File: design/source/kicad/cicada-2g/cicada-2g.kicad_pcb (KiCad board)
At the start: 2 copper layers, 40 x 65 mm, 52 parts, among them J2 Host, J3 USB_OTG, J4 IPX, J5 IPX, P1 SK-C793, Q1 NMOS, Q2 NMOS, Q4 NMOS, U2 USBLC6-2SC6, U3 M3406-ADJ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

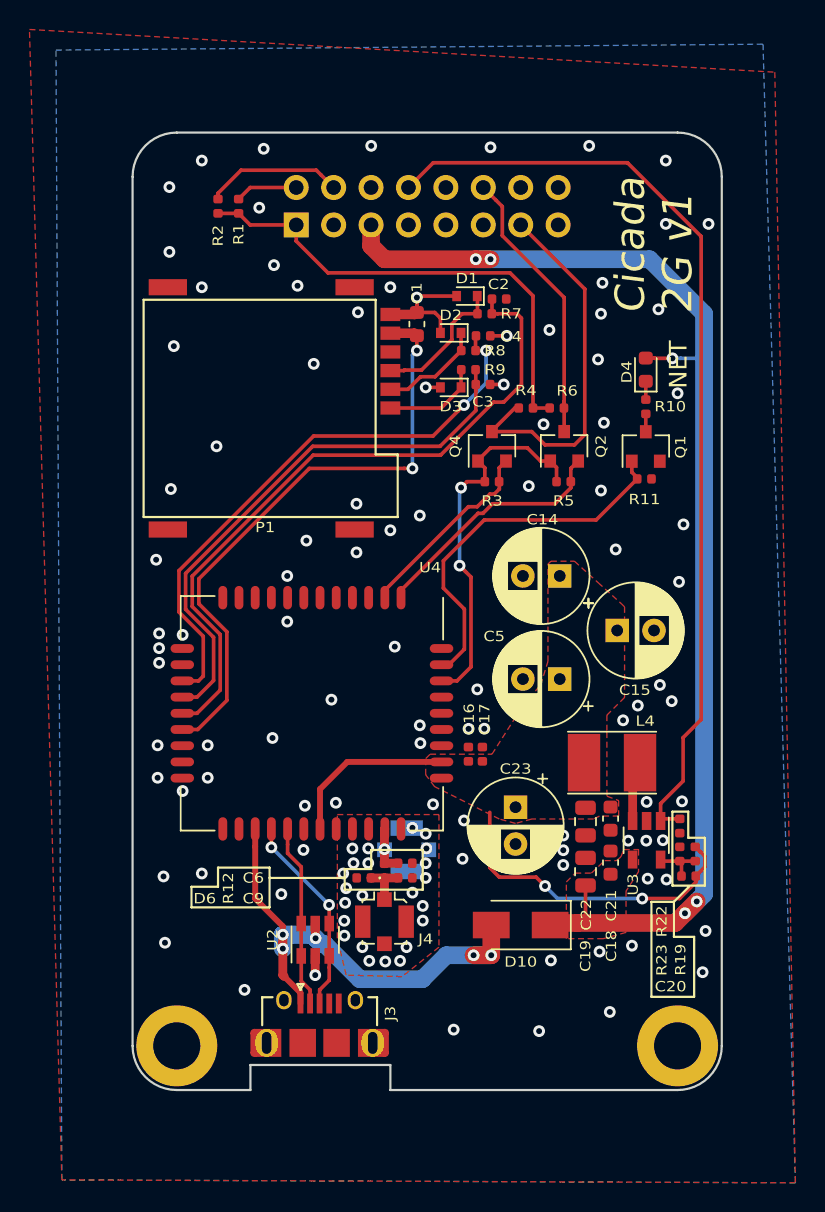
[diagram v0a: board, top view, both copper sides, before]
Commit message: Cicada 2G v2.1 - don't swap RX-TX
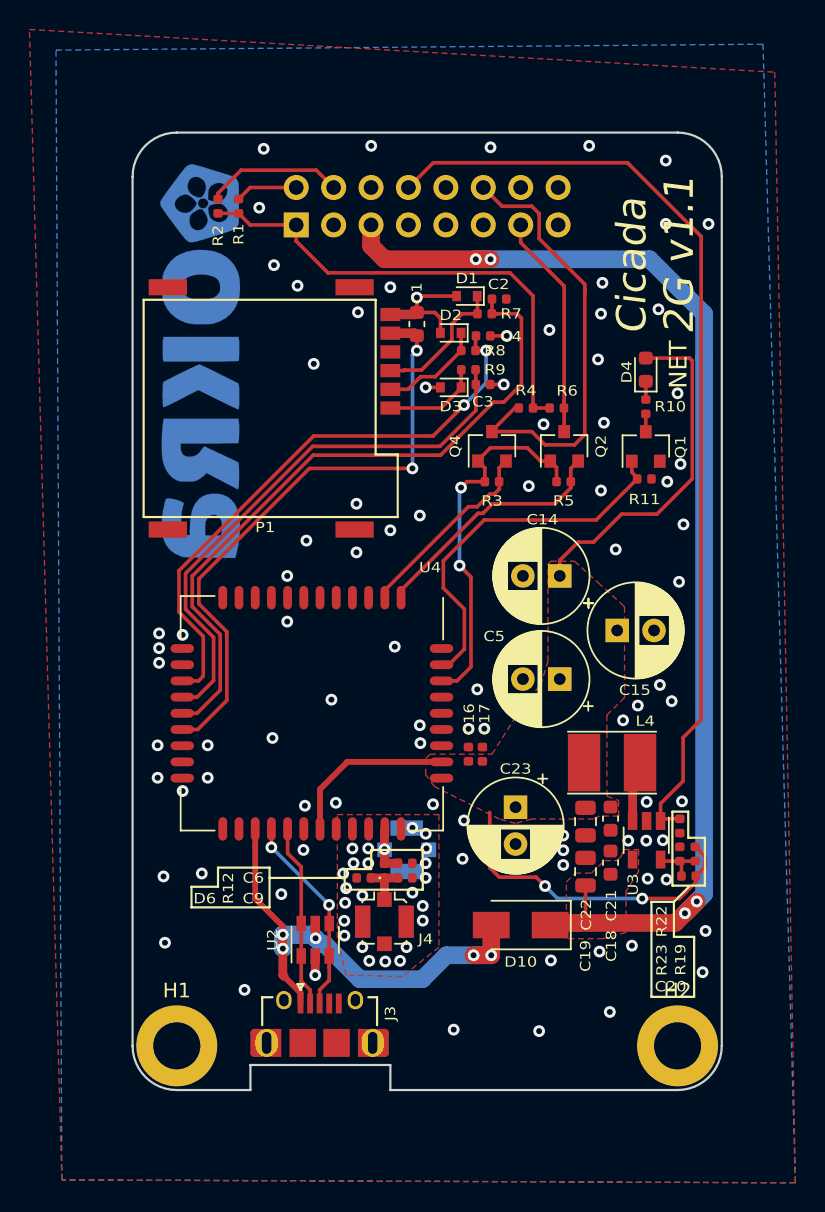
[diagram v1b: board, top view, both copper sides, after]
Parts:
- added LOGO1: SYM_Hot_Small, cicada-footprints:okra_logo_copper_2, B.Cu at (115.6, 75.5)
- R10: value 220R -> 470R
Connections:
- D4 pad 2: /5v -> /V_BATT
- Q2 pad 3: /UART_RX_3v3 -> /UART_TX_3v3
- Q4 pad 3: /UART_TX_3v3 -> /UART_RX_3v3
- R4 pad 2: /UART_TX_3v3 -> /UART_RX_3v3
- R6 pad 2: /UART_RX_3v3 -> /UART_TX_3v3
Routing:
- net /V_BATT: track 33.7 -> 57.3 mm
- net /UART_RX_3v3: track 18.9 -> 30.6 mm
- net /UART_TX_3v3: track 25.5 -> 15.3 mm
- net /5v: track 85.5 -> 81.6 mm, vias 5 -> 4
- net GND: vias 119 -> 113
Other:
- board text added: "Cicada 2G v1.1"
- board text removed: "Cicada 2G v1"

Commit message: Remove OKRA logo from PCB
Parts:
- removed LOGO1: SYM_Hot_Small, cicada-footprints:okra_logo_copper_2

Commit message: Updated PCB
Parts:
- removed C15, C23: 330uF 6.3v, Capacitor_THT:CP_Radial_D6.3mm_P2.50mm
- removed Q2, Q4: NMOS, Package_TO_SOT_SMD:SOT-23
- removed R11: 40.2k, Resistor_SMD:R_0402_1005Metric
- removed R5, R6: 4.7k, Resistor_SMD:R_0402_1005Metric
- added  : TestPoint, TestPoint:TestPoint_Pad_D1.5mm, F.Cu at (149.5, 78.8)
- added 5V: TestPoint, TestPoint:TestPoint_Pad_D1.5mm, F.Cu at (130.0, 68.8)
- added C10: 1000uF 10v, Capacitor_THT:CP_Radial_D8.0mm_P3.50mm, F.Cu at (148.3, 91.2)
- added C11: 1000uF 10v, Capacitor_THT:CP_Radial_D8.0mm_P3.50mm, F.Cu at (139.9, 98.0)
- added C12: 1000uF 10v, Capacitor_THT:CP_Radial_D8.0mm_P3.50mm, F.Cu at (145.6, 82.9)
- added C7: DNP, Capacitor_SMD:C_0402_1005Metric, F.Cu at (126.4, 89.6)
- added C8: DNP, Capacitor_SMD:C_0402_1005Metric, F.Cu at (136.1, 82.8)
- added D5: M2, Diode_SMD:D_SMA, F.Cu at (137.3, 118.7)
- added LOGO1: SYM_Hot_Small, cicada-footprints:okra_logo_copper_2, B.Cu at (115.3, 75.5)
- added R13: 0R, Resistor_SMD:R_0402_1005Metric, F.Cu at (134.8, 93.8)
- added R14: 6.98k, Resistor_SMD:R_0402_1005Metric, F.Cu at (142.8, 117.7)
- added TP1: TestPoint, TestPoint:TestPoint_Pad_D1.5mm, F.Cu at (131.5, 89.1)
- added U1: 74LVC1G17, Package_TO_SOT_SMD:SOT-353_SC-70-5, F.Cu at (134.0, 84.0)
- added U5: 74LVC1G17, Package_TO_SOT_SMD:SOT-353_SC-70-5, F.Cu at (130.7, 85.4)
- added V_BATT: TestPoint, TestPoint:TestPoint_Pad_D1.5mm, F.Cu at (138.4, 110.5)
- C14, C5: value 330uF 6.3v -> 1000uF 10v; footprint Capacitor_THT:CP_Radial_D6.3mm_P2.50mm -> Capacitor_THT:CP_Radial_D8.0mm_P3.50mm
- J2: footprint Connector_PinSocket_2.54mm:PinSocket_2x08_P2.54mm_Vertical -> Connector_PinSocket_2.54mm:PinSocket_2x10_P2.54mm_Vertical
- Q1: value NMOS -> BC847C
- R1: value DNP -> 150k
- R10: value 470R -> 330R
- R2: value 340k -> 150k
- R3, R4: value 4.7k -> 330R
- moved R3 9.35 mm to (128.1, 89.5), turned to 270 degrees
- moved C5 8.66 mm to (148.3, 99.7)
- moved R2 8.50 mm to (124.6, 61.7), turned to 0 degrees
- moved Q1 8.10 mm to (141.4, 74.5), turned to 0 degrees
- moved C22 6.73 mm to (135.1, 107.5)
- moved C21 6.70 mm to (136.8, 107.7)
- moved R10 5.60 mm to (140.4, 77.3)
- moved R1 5.53 mm to (122.6, 61.7), turned to 180 degrees
- moved L4 3.99 mm to (140.9, 105.8)
- moved R4 3.85 mm to (134.9, 81.4), turned to 270 degrees
- moved J2 2.54 mm to (119.6, 66.3)
- moved D4 1.66 mm to (144.3, 75.4), turned to 270 degrees
- moved C14 0.60 mm to (139.9, 89.5)
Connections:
- C5 pad 1: /V_BATT -> /5v
- J2 pad 1: /3v3 -> Net-(J2-Pad1)
- J2 pad 10: /SPI_CLK_3v3 -> /POWER
- J2 pad 11: /SPI_MOSI_3v3 -> /SPI_MISO_3v3
- J2 pad 12: /UART_RX_3v3 -> /SPI_CLK_3v3
- J2 pad 13: /UART_TX_3v3 -> /SPI_MOSI_3v3
- J2 pad 14: /nCS_WIFI -> /UART_RX_3v3
- J2 pad 15: /nCS_3G_3v3 -> /UART_TX_3v3
- J2 pad 16: /nRST -> /nCS_WIFI
- J2 pad 2: /VER_1 -> Net-(J2-Pad2)
- J2 pad 3: GND -> /3v3
- J2 pad 4: /VER_2 -> /VER_1
- J2 pad 5: /5v -> GND
- J2 pad 6: GND -> /VER_2
- J2 pad 7: GND -> /5v
- J2 pad 8: /POWER -> GND
- J2 pad 9: /SPI_MISO_3v3 -> GND
- Q1 pad 2: GND -> Net-(Q1-Pad2)
- Q1 pad 3: Net-(Q1-Pad3) -> Net-(D4-Pad1)
- R10 pad 1: Net-(D4-Pad1) -> Net-(Q1-Pad2)
- R10 pad 2: Net-(Q1-Pad3) -> GND
- R3 pad 1: /2v8 -> Net-(R3-Pad1)
- R4 pad 1: /3v3 -> /UART_TX_3v3
- R4 pad 2: /UART_RX_3v3 -> Net-(R4-Pad2)
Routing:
- net /5v: track 81.6 -> 224.7 mm, vias 4 -> 6
- net /POWER: track 64.8 -> 80.9 mm, vias 0 -> 1
- net /UART_RX_2v8: track 13.2 -> 2.91 mm
- net /2v8: track 25.6 -> 15.9 mm
- net /V_BATT: track 57.3 -> 48.4 mm
- net /VER_2: track 9.38 -> 2.22 mm
- net /UART_TX_2v8: track 16.9 -> 9.86 mm
- net Net-(TP1-Pad1): track 0.00 -> 6.09 mm
- net Net-(R13-Pad1): track 0.00 -> 5.48 mm
- net /UART_RX_3v3: track 30.6 -> 25.2 mm
- net Net-(R3-Pad1): track 0.00 -> 4.22 mm
- net GND: track 12.7 -> 16.4 mm, vias 113 -> 111
- net Net-(D5-Pad1): track 0.00 -> 3.37 mm
- net /UART_TX_3v3: track 15.3 -> 18.5 mm
- net /VBUS: track 36.5 -> 39.3 mm
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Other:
- board text added: "Cicada 2G v1.2"
- board text removed: "Cicada 2G v1.1"

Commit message: Generated manufacturing package
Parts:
- C10: value 1000uF 10v -> DNP 1000uF 10v
- D5: value M2 -> SS14
- J5: value IPX -> DNP IPX
- Q1: value BC847C -> 2N7002
- R10: value 330R -> 1K
- TP2: renamed from  
- moved LOGO1 3.80 mm to (114.6, 79.3)
- renumbered 5V to TP3, V_BATT to TP4
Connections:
- Q1 pad 2: Net-(Q1-Pad2) -> GND
- Q1 pad 3: Net-(D4-Pad1) -> Net-(Q1-Pad3)
- R10 pad 1: Net-(Q1-Pad2) -> Net-(Q1-Pad3)
- R10 pad 2: GND -> Net-(D4-Pad1)
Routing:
- net GND: track 16.4 -> 22.8 mm, vias 111 -> 112
- net Net-(D4-Pad1): track 1.95 -> 5.85 mm
- net Net-(Q1-Pad3): track 0.00 -> 3.77 mm
- net Net-(Q1-Pad2): track 1.37 -> 0.00 mm
- net (no net): vias 2 -> 0

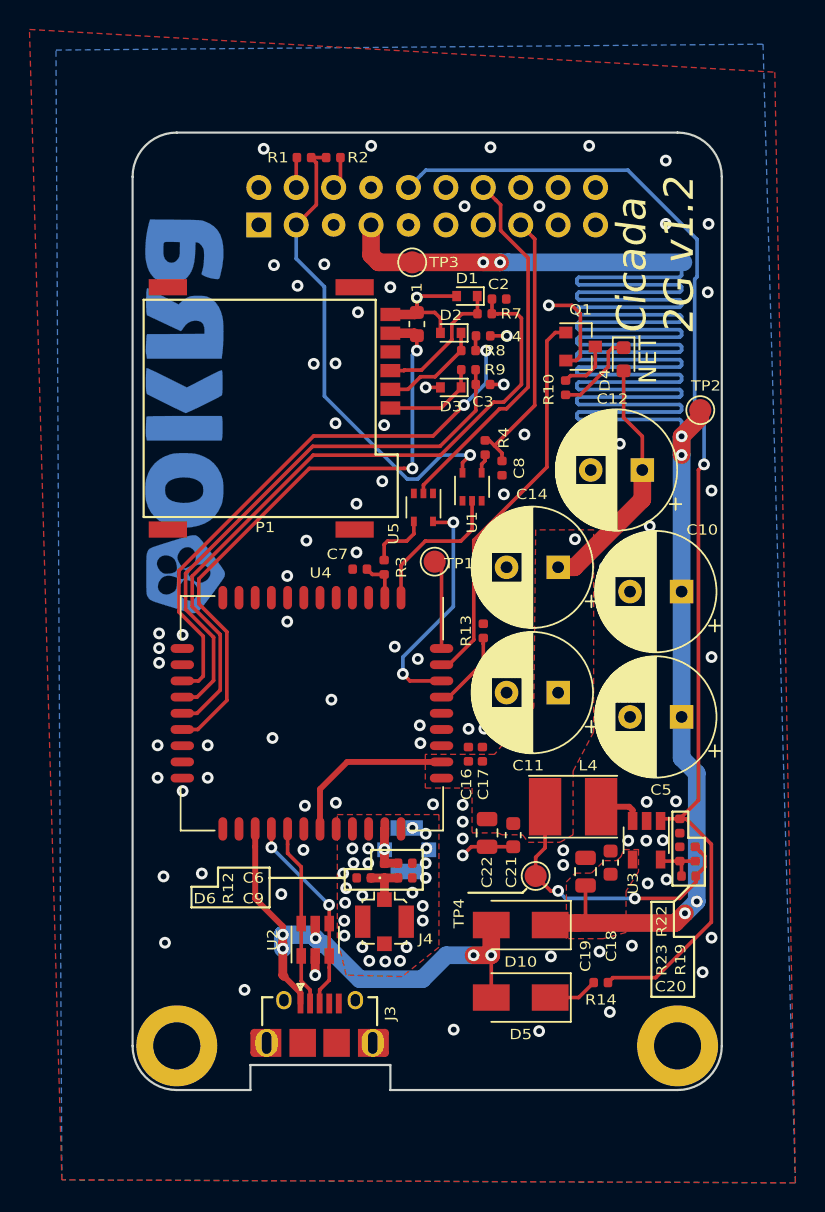
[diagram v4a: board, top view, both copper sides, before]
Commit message: Clean up the component libraries
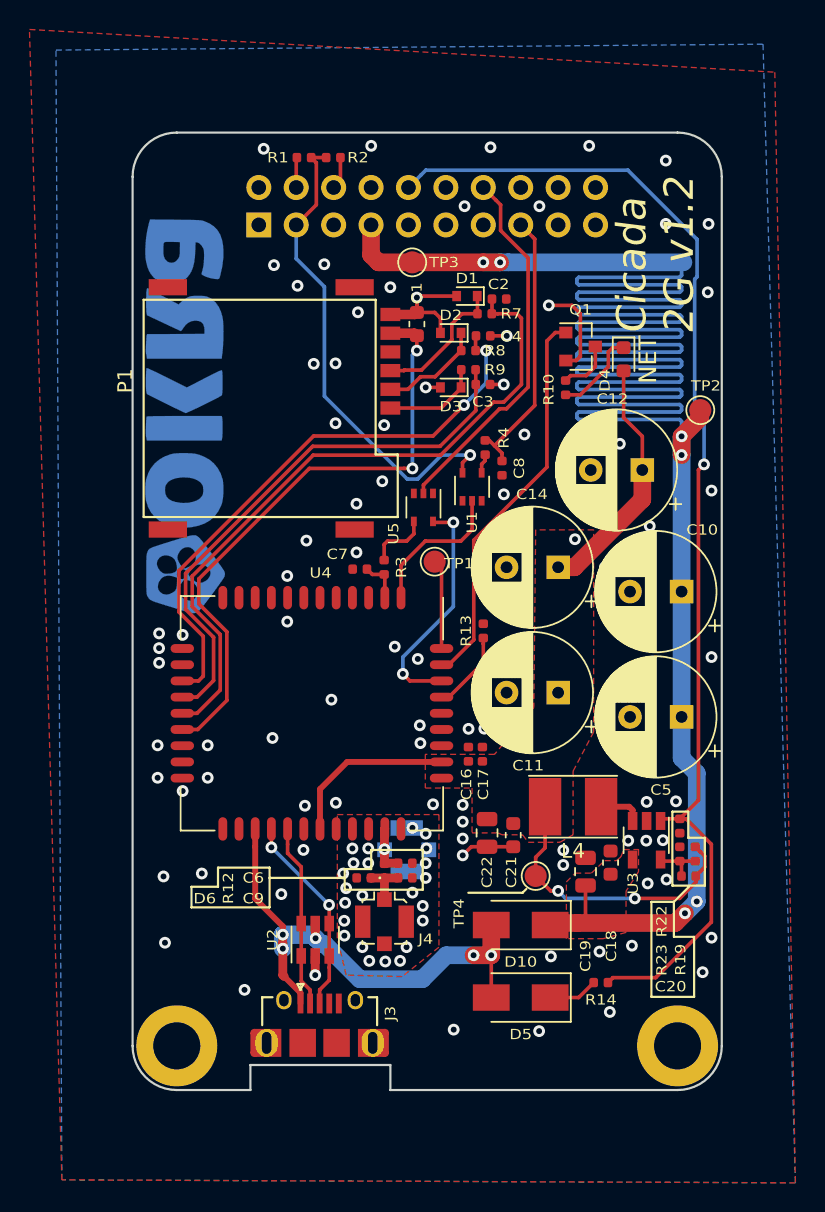
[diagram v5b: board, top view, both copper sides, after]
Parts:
- L4: footprint Inductor_SMD:L_Taiyo-Yuden_NR-40xx_HandSoldering -> cicada-footprints:L_4030_Handsoldering
- P1: footprint sk-c793:SK-C793 -> cicada-footprints:SK-C793
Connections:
- H1 pad 1: Net-(H1-Pad1) -> (no net)
- H2 pad 1: Net-(H2-Pad1) -> (no net)
- J2 pad 1: Net-(J2-Pad1) -> (no net)
- J2 pad 11: /SPI_MISO_3v3 -> (no net)
- J2 pad 12: /SPI_CLK_3v3 -> (no net)
- J2 pad 13: /SPI_MOSI_3v3 -> (no net)
- J2 pad 16: /nCS_WIFI -> (no net)
- J2 pad 17: /nCS_3G_3v3 -> (no net)
- J2 pad 18: /nRST -> (no net)
- J2 pad 19: Net-(J2-Pad19) -> (no net)
- J2 pad 2: Net-(J2-Pad2) -> (no net)
- J2 pad 20: Net-(J2-Pad20) -> (no net)
- J3 pad 4: Net-(J3-Pad4) -> (no net)
- P1 pad 6: Net-(P1-Pad6) -> (no net)
- U4 pad 10: Net-(U4-Pad10) -> (no net)
- U4 pad 11: Net-(U4-Pad11) -> (no net)
- U4 pad 12: Net-(U4-Pad12) -> (no net)
- U4 pad 14: Net-(U4-Pad14) -> (no net)
- U4 pad 20: Net-(U4-Pad20) -> (no net)
- U4 pad 22: Net-(U4-Pad22) -> (no net)
- U4 pad 23: Net-(U4-Pad23) -> (no net)
- U4 pad 29: Net-(U4-Pad29) -> (no net)
- U4 pad 3: Net-(U4-Pad3) -> (no net)
- U4 pad 38: Net-(U4-Pad38) -> (no net)
- U4 pad 4: Net-(U4-Pad4) -> (no net)
- U4 pad 5: Net-(U4-Pad5) -> (no net)
- U4 pad 6: Net-(U4-Pad6) -> (no net)
- U4 pad 7: Net-(U4-Pad7) -> (no net)
- U4 pad 9: Net-(U4-Pad9) -> (no net)

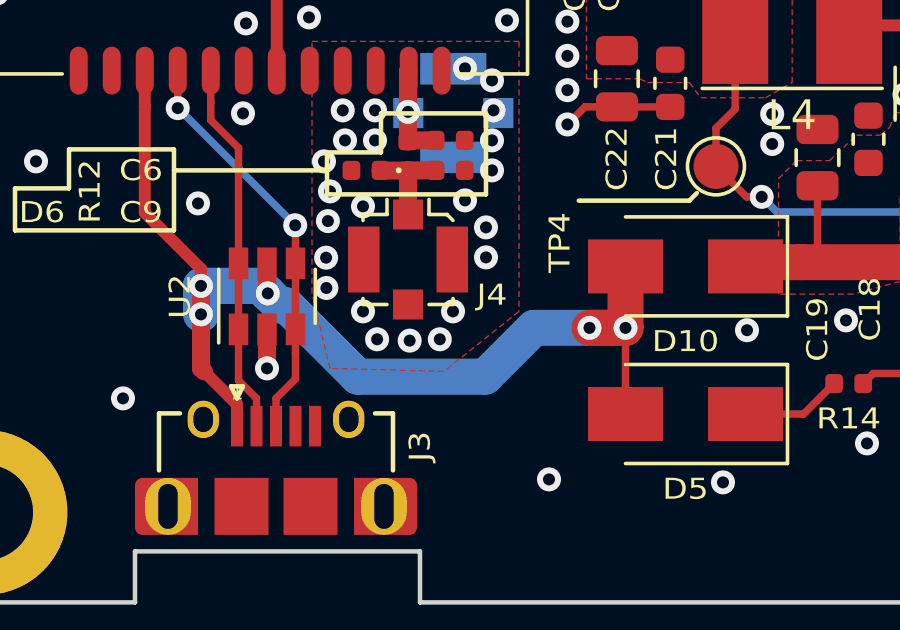
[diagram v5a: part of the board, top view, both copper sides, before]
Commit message: Update the library directory structure to match other Okra projects
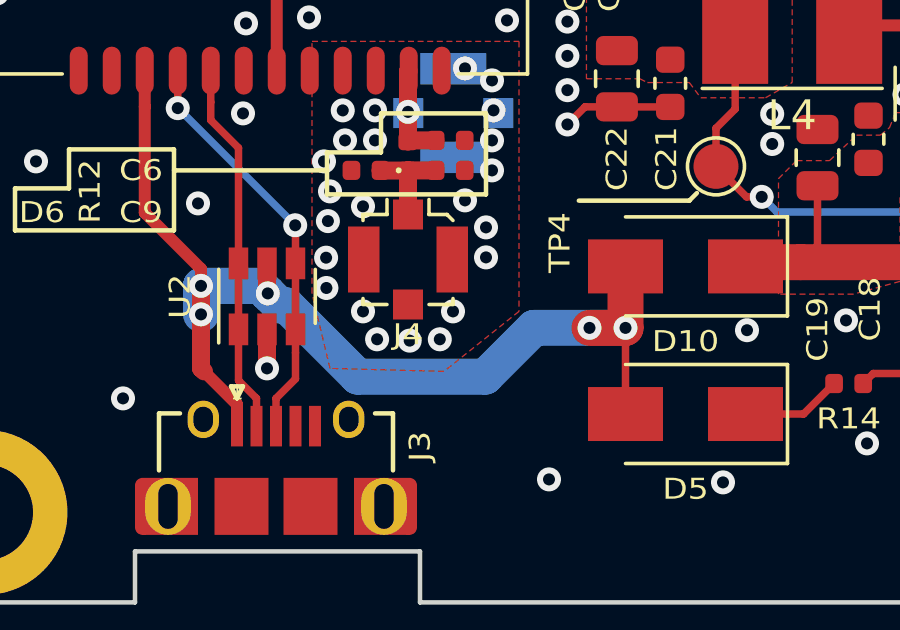
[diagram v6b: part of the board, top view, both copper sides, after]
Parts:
- J4, J5: footprint Connector_Coaxial:U.FL_Molex_MCRF_73412-0110_Vertical -> cicada-footprints:U.FL_Molex_MCRF_73412-0110_Vertical
